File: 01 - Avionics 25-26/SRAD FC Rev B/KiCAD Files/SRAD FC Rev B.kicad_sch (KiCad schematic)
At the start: 0 parts

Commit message: wired microcontroller pins
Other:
- sheet Microcontroller ports: added none; removed NRST
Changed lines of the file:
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@@
-			)
-		)
-		(pin "NRST" input
-			(at 53.34 147.32 270)
-			(effects
-				(font
-					(size 1.27 1.27)
-				)
-				(justify left)
 			)
 		)

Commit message: added power as hierarchical sheet pins
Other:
- sheet Barometer ports: added BARO_1.8V-3.6V_POWER; removed none
- sheet GPS ports: added GPS_3.3V_POWER; removed none
- sheet High G Accelerometer ports: added ACCEL_2.5V_POWER_SENSITIVE, ACCEL_3.3V_POWER; removed none
- sheet IMU ports: added IMU_1.71V-1.95V_POWER_VDD, IMU_1.71V-1.95V_POWER_VDDIO; removed none
- sheet RF Module ports: added RF_3.3V_POWER; removed none
- sheet Storage ports: added FLASH_3.3V_POWER; removed none
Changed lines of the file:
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@@
 		(rev "B")
 		(company "Missouri S&T Rocket Design Team")
-		(comment 1 "Author(s): Aaron Brinker, Isaac Lough, Joseph Hinchie, Ryan Newey, and Ian Butrick")
+		(comment 1 "Author(s): Aaron Brinker, Isaac Lough, Joseph Hinchie, Ryan Newey, Ian Butrick, and Adam Seals")
 	)
 	(junction
@@
 			)
 		)
+		(pin "FLASH_3.3V_POWER" input
+			(at 199.39 111.76 0)
+			(effects
+				(font
+					(size 1.27 1.27)
+				)
+				(justify right)
+			)
+		)
 		(instances
 			(project "SRAD FC Rev B"
@@
 			)
 		)
+		(pin "ACCEL_2.5V_POWER_SENSITIVE" input
+			(at 275.59 60.96 0)
+			(effects
+				(font
+					(size 1.27 1.27)
+				)
+				(justify right)
+			)
+		)
+		(pin "ACCEL_3.3V_POWER" input
+			(at 275.59 58.42 0)
+			(effects
+				(font
+					(size 1.27 1.27)
+				)
+				(justify right)
+			)
+		)
 		(instances
 			(project "SRAD FC Rev B"
@@
 			)
 		)
+		(pin "GPS_3.3V_POWER" output
+			(at 274.32 152.4 0)
+			(effects
+				(font
+					(size 1.27 1.27)
+				)
+				(justify right)
+			)
+		)
 		(instances
 			(project "SRAD FC Rev B"
@@
 			)
 		)
+		(pin "RF_3.3V_POWER" input
+			(at 189.23 40.64 0)
+			(effects
+				(font
+					(size 1.27 1.27)
+				)
+				(justify right)
+			)
+		)
 		(instances
 			(project "SRAD FC Rev B"
@@
 			)
 		)
+		(pin "IMU_1.71V-1.95V_POWER_VDDIO" input
+			(at 149.86 106.68 0)
+			(effects
+				(font
+					(size 1.27 1.27)
+				)
+				(justify right)
+			)
+		)
+		(pin "IMU_1.71V-1.95V_POWER_VDD" input
+			(at 149.86 109.22 0)
+			(effects
+				(font
+					(size 1.27 1.27)
+				)
+				(justify right)
+			)
+		)
 		(instances
 			(project "SRAD FC Rev B"
@@
 			)
 		)
+		(pin "BARO_1.8V-3.6V_POWER" input
+			(at 138.43 44.45 0)
+			(effects
+				(font
+					(size 1.27 1.27)
+				)
+				(justify right)
+			)
+		)

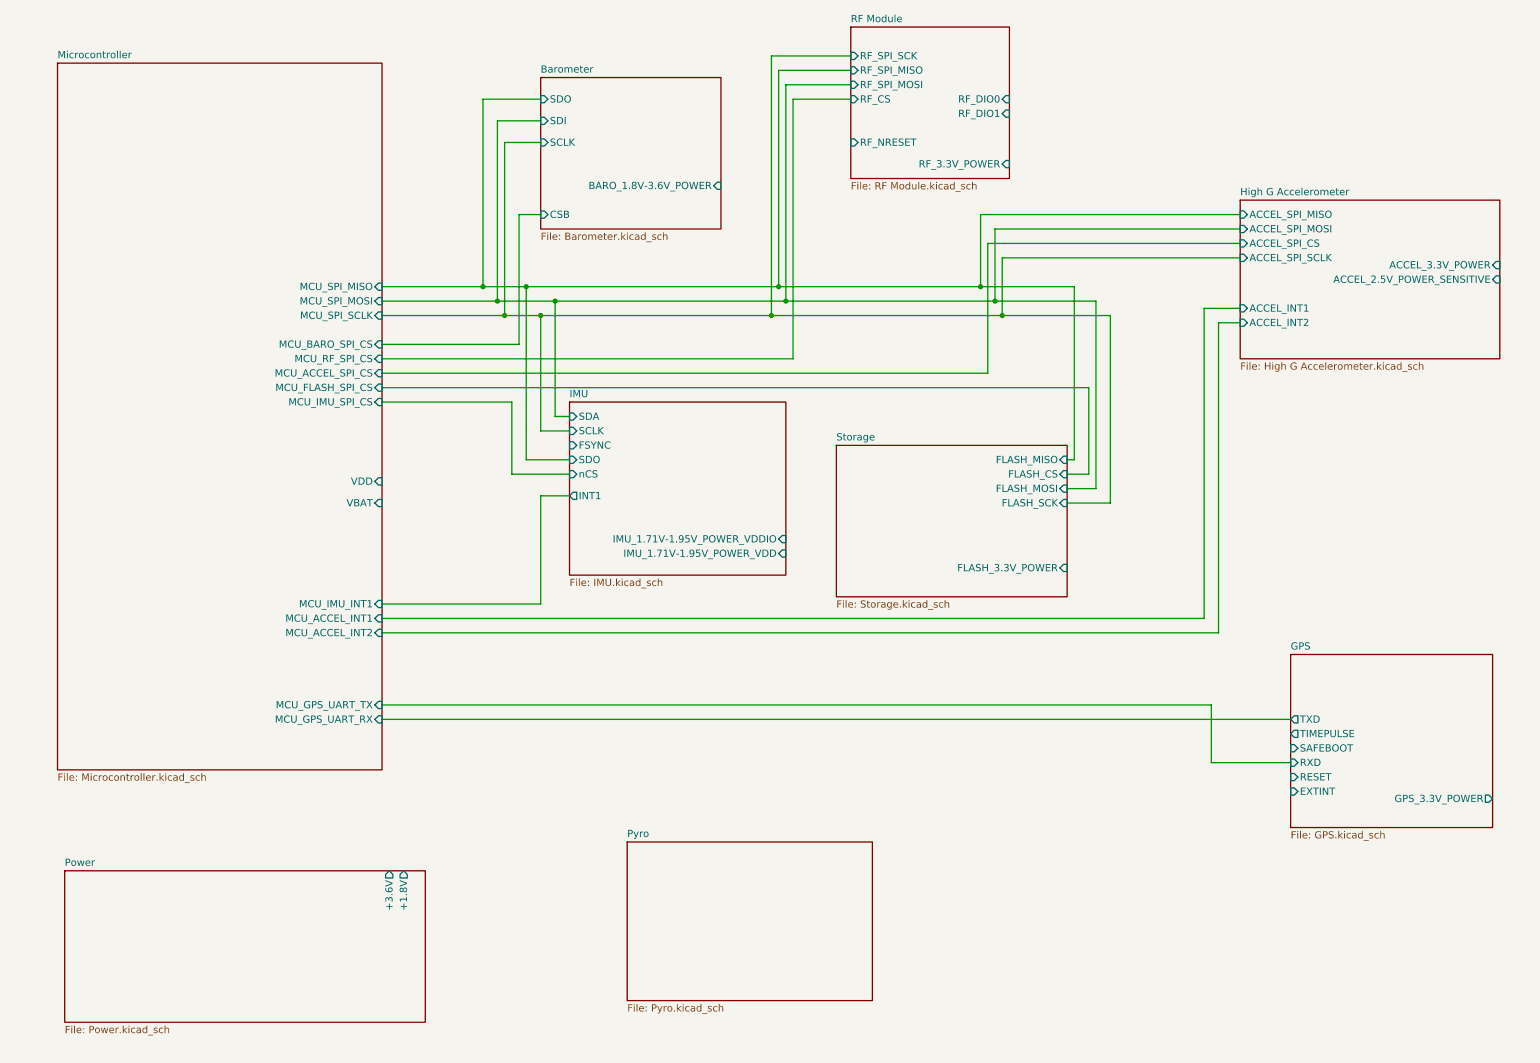
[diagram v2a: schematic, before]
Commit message: wired power on top level sheet
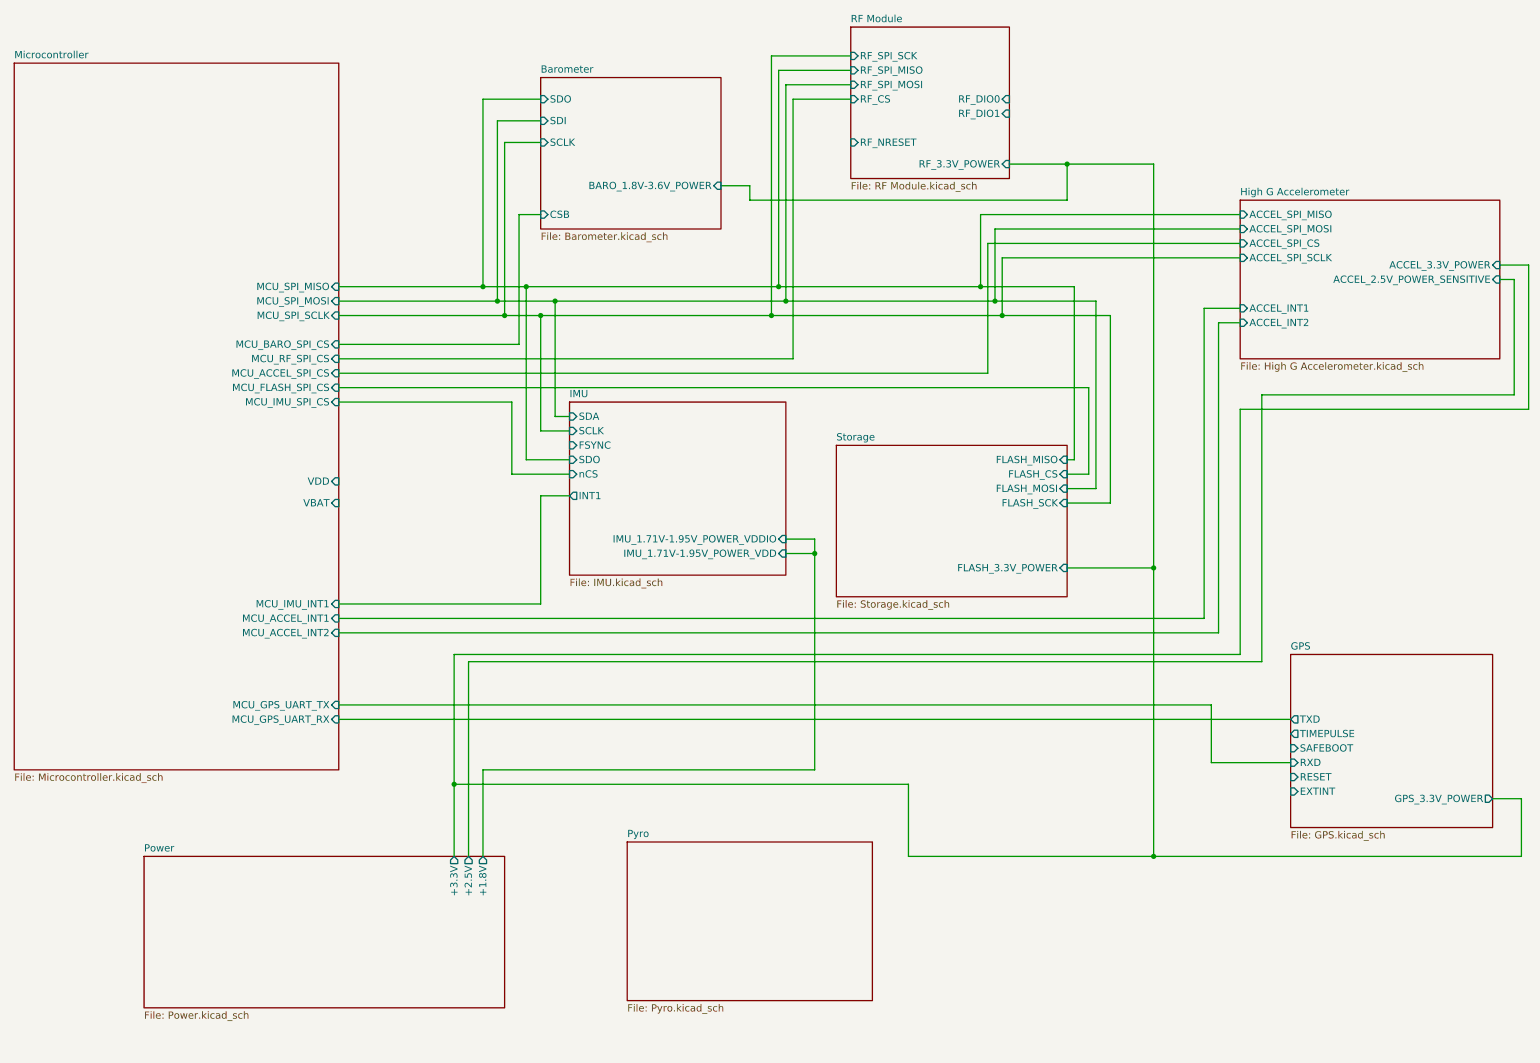
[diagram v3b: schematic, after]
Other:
- sheet Power ports: added +2.5V, +3.3V; removed +3.6V

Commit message: imported pyro from revision A
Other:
- sheet Pyro ports: added ARMED, CH1_DETECT, CH1_FIRE, CH2_DETECT, CH2_FIRE, CURRENT_SENSE, VBAT; removed none
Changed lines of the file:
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@@
+			)
+		)
+		(pin "CURRENT_SENSE" output
+			(at 121.92 185.42 180)
+			(effects
+				(font
+					(size 1.27 1.27)
+				)
+				(justify left)
+			)
+		)
+		(pin "CH1_DETECT" output
+			(at 121.92 168.91 180)
+			(effects
+				(font
+					(size 1.27 1.27)
+				)
+				(justify left)
+			)
+		)
+		(pin "CH2_DETECT" output
+			(at 121.92 171.45 180)
+			(effects
+				(font
+					(size 1.27 1.27)
+				)
+				(justify left)
+			)
+		)
+		(pin "CH1_FIRE" input
+			(at 121.92 176.53 180)
+			(effects
+				(font
+					(size 1.27 1.27)
+				)
+				(justify left)
+			)
+		)
+		(pin "ARMED" output
+			(at 121.92 163.83 180)
+			(effects
+				(font
+					(size 1.27 1.27)
+				)
+				(justify left)
+			)
+		)
+		(pin "CH2_FIRE" input
+			(at 121.92 179.07 180)
+			(effects
+				(font
+					(size 1.27 1.27)
+				)
+				(justify left)
+			)
+		)
+		(pin "VBAT" input
+			(at 165.1 162.56 0)
+			(effects
+				(font
+					(size 1.27 1.27)
+				)
+				(justify right)
 			)
 		)
